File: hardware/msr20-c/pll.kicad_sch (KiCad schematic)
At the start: 0 parts

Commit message: add pll to schematic
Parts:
- added C5, C7, C9: 1n, Capacitor_SMD:C_0805_2012Metric, symbol Device:C
- added C6: 47p, Capacitor_SMD:C_0805_2012Metric, symbol Device:C
- added C8: 100p, Capacitor_SMD:C_0805_2012Metric, symbol Device:C
- added R2: 3.3k, Resistor_SMD:R_0805_2012Metric, symbol Device:R
- added R3: 33k, Resistor_SMD:R_0805_2012Metric, symbol Device:R
- added TP1, TP2: TestPoint, TestPoint:TestPoint_Pad_D1.0mm, symbol Connector:TestPoint
- added U6: 74LS163, Package_DIP:DIP-16_W7.62mm_LongPads, symbol msr20:74LS163
- added U7: CD74HC4046, Package_DIP:DIP-16_W7.62mm_LongPads, symbol msr20:CD74HC4046
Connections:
- new net: R3.1, U7.2 (PC1)
- new net: C8.2, R3.2, U7.9 (VCO-I)
- new net: C6.1, U7.7 (C1B)
- new net: C6.2, U7.6 (C1A)
- new net: TP2.1, U6.11 (Qd), U7.3 (COMP)
- new net: C9.1, TP1.1, U6.2 (CLK), U7.4 (VCO-O)
- new net: R2.2, U7.12 (R2)
- new net: C7.2, U7.11 (R1)
- new net: C5.2, U7.14 (SIG)
- new net +5V: U6.1 (~{CLR}), U6.10 (ENT), U6.16 (VCC), U6.7 (ENP), U6.9 (~{LOAD}), U7.16 (VCC)
- new net GND: C7.1, C8.1, R2.1, U6.8 (GND), U7.8 (GND)
- new net IN: C5.1
- new net OUT: C9.2
- no-connect marks 0 -> 12
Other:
- title: (none) -> Phase-Locked Loop

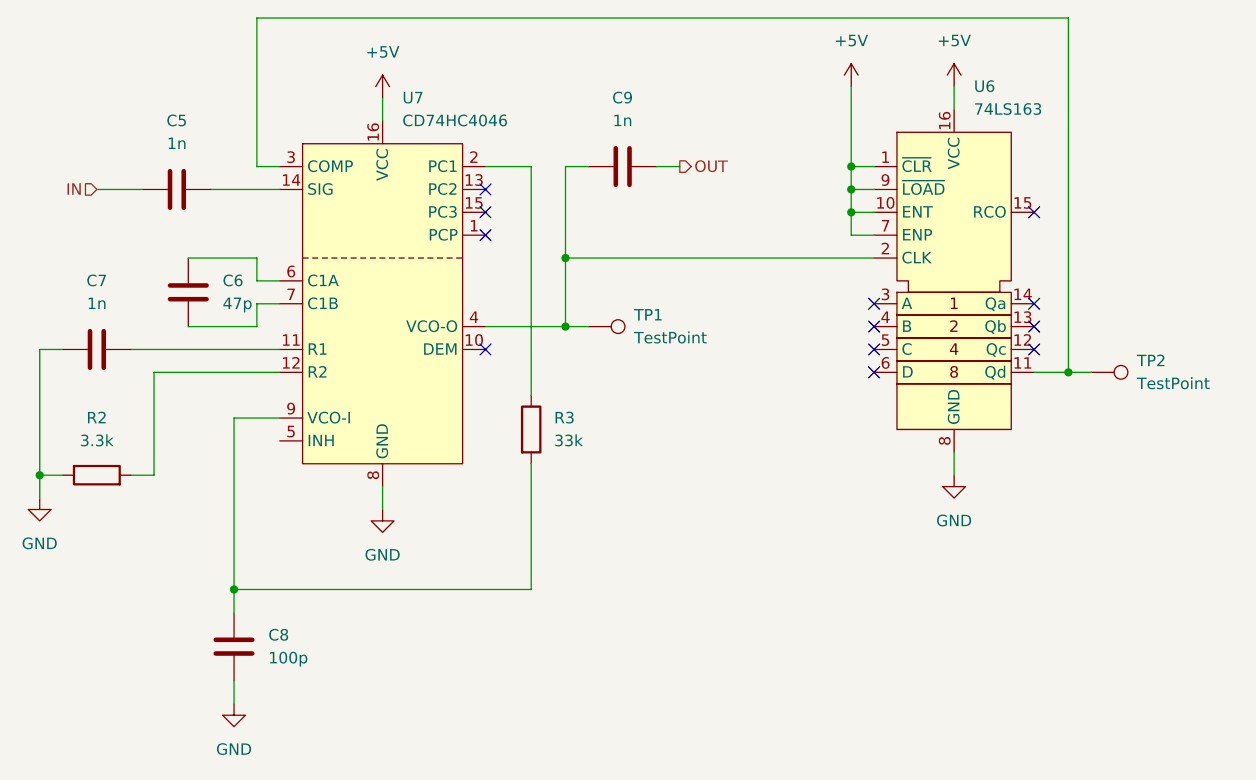
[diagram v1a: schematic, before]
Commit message: add power sheet, assign footprints
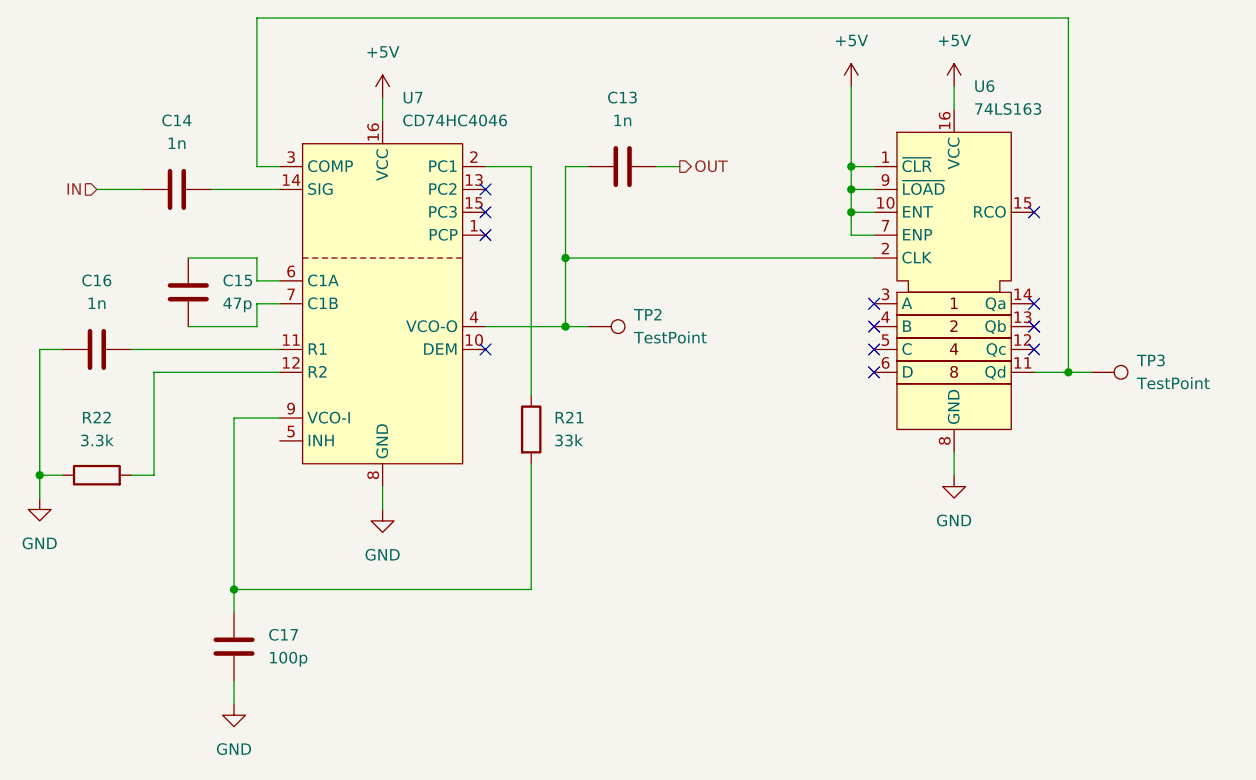
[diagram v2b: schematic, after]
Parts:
- renumbered C9 to C13, C5 to C14, C6 to C15, C7 to C16, C8 to C17, R3 to R21, R2 to R22, TP1 to TP2, TP2 to TP3
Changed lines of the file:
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@@
 		(dnp no)
 		(fields_autoplaced yes)
-		(property "Reference" "R3"
+		(property "Reference" "R21"
 			(at 120.65 104.1399 0)
 			(effects
@@
 			(project "msr20-c"
 				(path "/3d24e86e-b070-4f0e-8c28-04e9dd9d95d1/f1de7ee2-5c1c-4a91-a494-9460fbe8fb93"
-					(reference "R3")
+					(reference "R21")
 					(unit 1)
 				)
@@
 		(dnp no)
 		(fields_autoplaced yes)
-		(property "Reference" "#PWR022"
+		(property "Reference" "#PWR052"
 			(at 63.5 119.38 0)
 			(effects
@@
 			(project "msr20-c"
 				(path "/3d24e86e-b070-4f0e-8c28-04e9dd9d95d1/f1de7ee2-5c1c-4a91-a494-9460fbe8fb93"
-					(reference "#PWR022")
+					(reference "#PWR052")
 					(unit 1)
 				)
@@
 		(dnp no)
 		(fields_autoplaced yes)
-		(property "Reference" "C6"
+		(property "Reference" "C15"
 			(at 83.82 88.8999 0)
 			(effects
@@
 			(project "msr20-c"
 				(path "/3d24e86e-b070-4f0e-8c28-04e9dd9d95d1/f1de7ee2-5c1c-4a91-a494-9460fbe8fb93"
-					(reference "C6")
+					(reference "C15")
 					(unit 1)
 				)
@@
 		(dnp no)
 		(fields_autoplaced yes)
-		(property "Reference" "R2"
+		(property "Reference" "R22"
 			(at 69.85 104.14 90)
 			(effects
@@
 			(project "msr20-c"
 				(path "/3d24e86e-b070-4f0e-8c28-04e9dd9d95d1/f1de7ee2-5c1c-4a91-a494-9460fbe8fb93"
-					(reference "R2")
+					(reference "R22")
 					(unit 1)
 				)
@@
 		(dnp no)
 		(fields_autoplaced yes)
-		(property "Reference" "TP2"
+		(property "Reference" "TP3"
 			(at 185.42 97.7899 90)
 			(effects
@@
 			(project "msr20-c"
 				(path "/3d24e86e-b070-4f0e-8c28-04e9dd9d95d1/f1de7ee2-5c1c-4a91-a494-9460fbe8fb93"
-					(reference "TP2")
+					(reference "TP3")
 					(unit 1)
 				)
@@
 		(dnp no)
 		(fields_autoplaced yes)
-		(property "Reference" "#PWR020"
+		(property "Reference" "#PWR053"
 			(at 101.6 120.65 0)
 			(effects
@@
 			(project "msr20-c"
 				(path "/3d24e86e-b070-4f0e-8c28-04e9dd9d95d1/f1de7ee2-5c1c-4a91-a494-9460fbe8fb93"
-					(reference "#PWR020")
+					(reference "#PWR053")
 					(unit 1)
 				)
@@
 		(dnp no)
 		(fields_autoplaced yes)
-		(property "Reference" "C7"
+		(property "Reference" "C16"
 			(at 69.85 88.9 90)
 			(effects
@@
 			(project "msr20-c"
 				(path "/3d24e86e-b070-4f0e-8c28-04e9dd9d95d1/f1de7ee2-5c1c-4a91-a494-9460fbe8fb93"
-					(reference "C7")
+					(reference "C16")
 					(unit 1)
 				)
@@
 		(dnp no)
 		(fields_autoplaced yes)
-		(property "Reference" "C8"
+		(property "Reference" "C17"
 			(at 88.9 128.2699 0)
 			(effects
@@
 			(project "msr20-c"
 				(path "/3d24e86e-b070-4f0e-8c28-04e9dd9d95d1/f1de7ee2-5c1c-4a91-a494-9460fbe8fb93"
-					(reference "C8")
+					(reference "C17")
 					(unit 1)
 				)
@@
 		(dnp no)
 		(fields_autoplaced yes)
-		(property "Reference" "C9"
+		(property "Reference" "C13"
 			(at 128.27 68.58 90)
 			(effects
@@
 			(project "msr20-c"
 				(path "/3d24e86e-b070-4f0e-8c28-04e9dd9d95d1/f1de7ee2-5c1c-4a91-a494-9460fbe8fb93"
-					(reference "C9")
+					(reference "C13")
 					(unit 1)
 				)
@@
 		(dnp no)
 		(fields_autoplaced yes)
-		(property "Reference" "#PWR09"
+		(property "Reference" "#PWR050"
 			(at 101.6 72.39 0)
 			(effects
@@
 			(project "msr20-c"
 				(path "/3d24e86e-b070-4f0e-8c28-04e9dd9d95d1/f1de7ee2-5c1c-4a91-a494-9460fbe8fb93"
-					(reference "#PWR09")
+					(reference "#PWR050")
 					(unit 1)
 				)
@@
 		(dnp no)
 		(fields_autoplaced yes)
-		(property "Reference" "#PWR023"
+		(property "Reference" "#PWR054"
 			(at 85.09 142.24 0)
 			(effects
@@
 			(project "msr20-c"
 				(path "/3d24e86e-b070-4f0e-8c28-04e9dd9d95d1/f1de7ee2-5c1c-4a91-a494-9460fbe8fb93"
-					(reference "#PWR023")
+					(reference "#PWR054")
 					(unit 1)
 				)
@@
 		(dnp no)
 		(fields_autoplaced yes)
-		(property "Reference" "#PWR021"
+		(property "Reference" "#PWR051"
 			(at 165.1 116.84 0)
 			(effects
@@
 			(project "msr20-c"
 				(path "/3d24e86e-b070-4f0e-8c28-04e9dd9d95d1/f1de7ee2-5c1c-4a91-a494-9460fbe8fb93"
-					(reference "#PWR021")
+					(reference "#PWR051")
 					(unit 1)
 				)
@@
 		(dnp no)
 		(fields_autoplaced yes)
-		(property "Reference" "TP1"
+		(property "Reference" "TP2"
 			(at 129.54 92.7099 90)
 			(effects
@@
 			(project "msr20-c"
 				(path "/3d24e86e-b070-4f0e-8c28-04e9dd9d95d1/f1de7ee2-5c1c-4a91-a494-9460fbe8fb93"
-					(reference "TP1")
+					(reference "TP2")
 					(unit 1)
 				)
@@
 		(dnp no)
 		(fields_autoplaced yes)
-		(property "Reference" "#PWR019"
+		(property "Reference" "#PWR049"
 			(at 165.1 71.12 0)
 			(effects
@@
 			(project "msr20-c"
 				(path "/3d24e86e-b070-4f0e-8c28-04e9dd9d95d1/f1de7ee2-5c1c-4a91-a494-9460fbe8fb93"
-					(reference "#PWR019")
+					(reference "#PWR049")
 					(unit 1)
 				)
@@
 		(dnp no)
 		(fields_autoplaced yes)
-		(property "Reference" "#PWR024"
+		(property "Reference" "#PWR048"
 			(at 153.67 71.12 0)
 			(effects
@@
 			(project "msr20-c"
 				(path "/3d24e86e-b070-4f0e-8c28-04e9dd9d95d1/f1de7ee2-5c1c-4a91-a494-9460fbe8fb93"
-					(reference "#PWR024")
+					(reference "#PWR048")
 					(unit 1)
 				)
@@
 		(dnp no)
 		(fields_autoplaced yes)
-		(property "Reference" "C5"
+		(property "Reference" "C14"
 			(at 78.74 71.12 90)
 			(effects
@@
 			(project "msr20-c"
 				(path "/3d24e86e-b070-4f0e-8c28-04e9dd9d95d1/f1de7ee2-5c1c-4a91-a494-9460fbe8fb93"
-					(reference "C5")
-					(unit 1)
-				)
+					(reference "C14")
+					(unit 1)
+				)

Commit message: pcb: pll, lna, rf-bpf layout
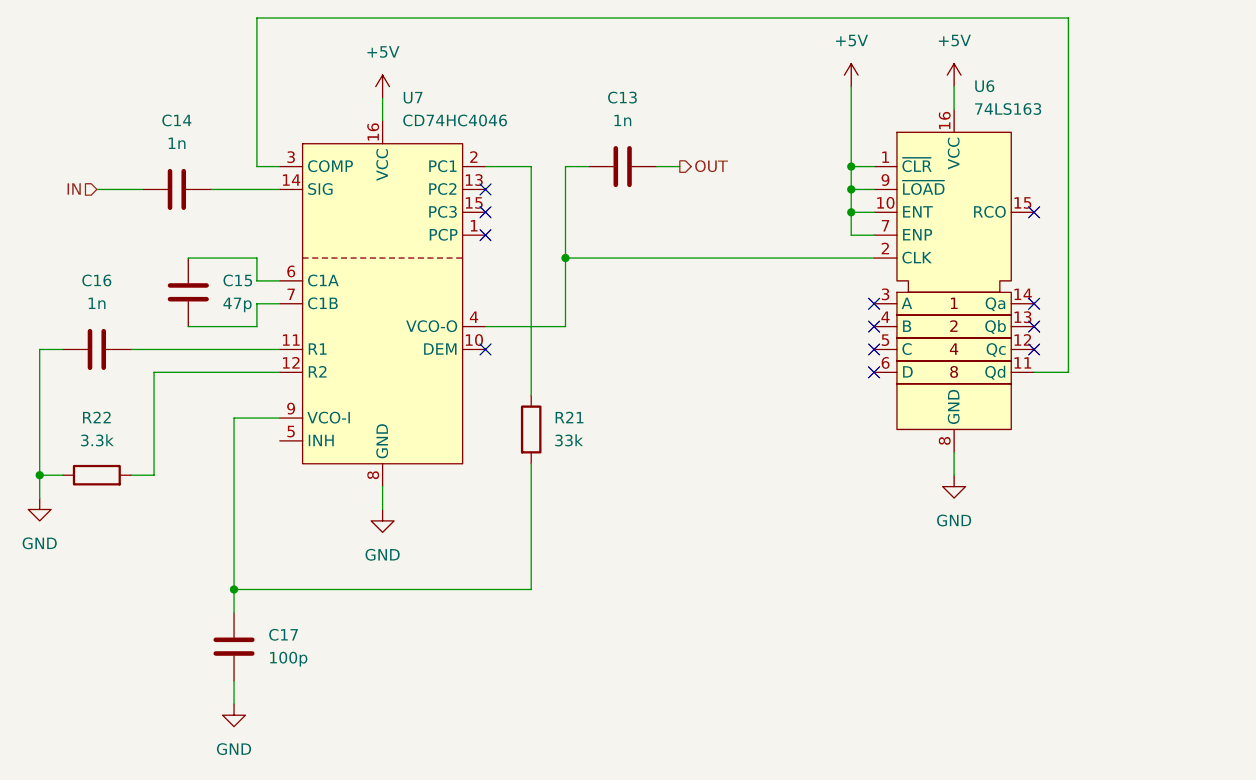
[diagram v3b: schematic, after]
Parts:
- removed TP2, TP3: TestPoint, TestPoint:TestPoint_Pad_D1.0mm, symbol Connector:TestPoint
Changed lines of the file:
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@@
-		(color 0 0 0 0)
-	)
-	(junction
-		(at 121.92 93.98)
-		(diameter 0)
-		(color 0 0 0 0)
-	)
-	(junction
-		(at 177.8 99.06)
-		(diameter 0)
 		(color 0 0 0 0)
 	)
@@
 	(wire
 		(pts
-			(xy 121.92 93.98) (xy 124.46 93.98)
-		)
-		(stroke
-			(width 0)
-			(type default)
-		)
-	)
-	(wire
-		(pts
 			(xy 121.92 86.36) (xy 156.21 86.36)
 		)
@@
 		(pts
 			(xy 85.09 123.19) (xy 85.09 125.73)
-		)
-		(stroke
-			(width 0)
-			(type default)
-		)
-	)
-	(wire
-		(pts
-			(xy 177.8 99.06) (xy 180.34 99.06)
 		)
 		(stroke
@@
 	)
 	(symbol
-		(lib_id "Connector:TestPoint")
-		(at 180.34 99.06 270)
-		(unit 1)
-		(exclude_from_sim no)
-		(in_bom yes)
-		(on_board yes)
-		(dnp no)
-		(fields_autoplaced yes)
-		(property "Reference" "TP3"
-			(at 185.42 97.7899 90)
-			(effects
-				(font
-					(size 1.27 1.27)
-				)
-				(justify left)
-			)
-		)
-		(property "Value" "TestPoint"
-			(at 185.42 100.3299 90)
-			(effects
-				(font
-					(size 1.27 1.27)
-				)
-				(justify left)
-			)
-		)
-		(property "Footprint" "TestPoint:TestPoint_Pad_D1.0mm"
-			(at 180.34 104.14 0)
-			(effects
-				(font
-					(size 1.27 1.27)
-				)
-				(hide yes)
-			)
-		)
-		(property "Datasheet" "~"
-			(at 180.34 104.14 0)
-			(effects
-				(font
-					(size 1.27 1.27)
-				)
-				(hide yes)
-			)
-		)
-		(property "Description" "test point"
-			(at 180.34 99.06 0)
-			(effects
-				(font
-					(size 1.27 1.27)
-				)
-				(hide yes)
-			)
-		)
-		(pin "1"
-		)
-		(instances
-			(project "msr20-c"
-				(path "/3d24e86e-b070-4f0e-8c28-04e9dd9d95d1/f1de7ee2-5c1c-4a91-a494-9460fbe8fb93"
-					(reference "TP3")
-					(unit 1)
-				)
-			)
-			(project "msr20"
-				(path "/827e4c90-6b76-4aba-b6da-8b66ea005818/879e4ab0-ee5d-4d03-b0f3-e28ce814003c"
-					(reference "TP2")
-					(unit 1)
-				)
-			)
-		)
-	)
-	(symbol
 		(lib_id "power:GND")
 		(at 101.6 114.3 0)
@@
 					(unit 1)
 				)
-			)
-		)
-	)
-	(symbol
-		(lib_id "Connector:TestPoint")
-		(at 124.46 93.98 270)
-		(unit 1)
-		(exclude_from_sim no)
-		(in_bom yes)
-		(on_board yes)
-		(dnp no)
-		(fields_autoplaced yes)
-		(property "Reference" "TP2"
-			(at 129.54 92.7099 90)
-			(effects
-				(font
-					(size 1.27 1.27)
-				)
-				(justify left)
-			)
-		)
-		(property "Value" "TestPoint"
-			(at 129.54 95.2499 90)
-			(effects
-				(font
-					(size 1.27 1.27)
-				)
-				(justify left)
-			)
-		)
-		(property "Footprint" "TestPoint:TestPoint_Pad_D1.0mm"
-			(at 124.46 99.06 0)
-			(effects
-				(font
-					(size 1.27 1.27)
-				)
-				(hide yes)
-			)
-		)
-		(property "Datasheet" "~"
-			(at 124.46 99.06 0)
-			(effects
-				(font
-					(size 1.27 1.27)
-				)
-				(hide yes)
-			)
-		)
-		(property "Description" "test point"
-			(at 124.46 93.98 0)
-			(effects
-				(font
-					(size 1.27 1.27)
-				)
-				(hide yes)
-			)
-		)
-		(pin "1"
-		)
-		(instances
-			(project "msr20-c"
-				(path "/3d24e86e-b070-4f0e-8c28-04e9dd9d95d1/f1de7ee2-5c1c-4a91-a494-9460fbe8fb93"
-					(reference "TP2")
-					(unit 1)
-				)
-			)
-			(project "msr20"
-				(path "/827e4c90-6b76-4aba-b6da-8b66ea005818/879e4ab0-ee5d-4d03-b0f3-e28ce814003c"
-					(reference "TP1")
-					(unit 1)
-				)

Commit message: finish pcb rev 1, new png render
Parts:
- added TP6: TestPoint, TestPoint:TestPoint_Pad_D1.0mm, symbol Connector:TestPoint
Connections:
- net at C13.1, U6.2 (CLK), U7.4 (VCO-O): now also TP6.1
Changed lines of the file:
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@@
+	)
+	(junction
+		(at 134.62 86.36)
+		(diameter 0)
+		(color 0 0 0 0)
 	)
 	(junction
@@
 	(wire
 		(pts
-			(xy 121.92 86.36) (xy 156.21 86.36)
+			(xy 121.92 86.36) (xy 134.62 86.36)
 		)
 		(stroke
@@
 	(wire
 		(pts
+			(xy 134.62 86.36) (xy 156.21 86.36)
+		)
+		(stroke
+			(width 0)
+			(type default)
+		)
+	)
+	(wire
+		(pts
 			(xy 153.67 81.28) (xy 153.67 78.74)
 		)
@@
 		(pts
 			(xy 90.17 88.9) (xy 87.63 88.9)
+		)
+		(stroke
+			(width 0)
+			(type default)
+		)
+	)
+	(wire
+		(pts
+			(xy 134.62 86.36) (xy 134.62 90.17)
 		)
 		(stroke
@@
 					(unit 1)
 				)
+			)
+		)
+	)
+	(symbol
+		(lib_id "Connector:TestPoint")
+		(at 134.62 90.17 180)
+		(unit 1)
+		(exclude_from_sim no)
+		(in_bom yes)
+		(on_board yes)
+		(dnp no)
+		(fields_autoplaced yes)
+		(property "Reference" "TP6"
+			(at 137.16 92.2019 0)
+			(effects
+				(font
+					(size 1.27 1.27)
+				)
+				(justify right)
+			)
+		)
+		(property "Value" "TestPoint"
+			(at 137.16 94.7419 0)
+			(effects
+				(font
+					(size 1.27 1.27)
+				)
+				(justify right)
+			)
+		)
+		(property "Footprint" "TestPoint:TestPoint_Pad_D1.0mm"
+			(at 129.54 90.17 0)
+			(effects
+				(font
+					(size 1.27 1.27)
+				)
+				(hide yes)
+			)
+		)
+		(property "Datasheet" "~"
+			(at 129.54 90.17 0)
+			(effects
+				(font
+					(size 1.27 1.27)
+				)
+				(hide yes)
+			)
+		)
+		(property "Description" "test point"
+			(at 134.62 90.17 0)
+			(effects
+				(font
+					(size 1.27 1.27)
+				)
+				(hide yes)
+			)
+		)
+		(pin "1"
+		)
+		(instances
+			(project "msr20-c"
+				(path "/3d24e86e-b070-4f0e-8c28-04e9dd9d95d1/f1de7ee2-5c1c-4a91-a494-9460fbe8fb93"
+					(reference "TP6")
+					(unit 1)
+				)
